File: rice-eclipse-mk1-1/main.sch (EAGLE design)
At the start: 146 parts, among them IC1 LMV321LICTRT, IC10 MCP6N11R, IC11 MCP6N11R, IC12 MCP6N11R, IC2 LMV321LICTRT, IC3 LMV321LICTRT, IC4 LMV321LICTRT, IC5 MCP6N11R, IC6 LMV321LICTRT, IC7 LMV321LICTRT, IC8 LMV321LICTRT, IC9 LMV321LICTRT, U6 1101M2S3CQE2

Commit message: Added AA filter to lowpass output.
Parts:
- added C10, C37, C40, C43, C46: 0.1UF, rcl:C-USC0805
- added C11, C36, C38, C39, C41, C42, C44, C45: 1nF, rcl:C-USC0805
- added C47, C48: ?, rcl:C-USC0805
- added IC13, IC14, IC15, IC16, IC17: LMV321LICTRT, st-microelectronics-extra:LMV321LICTRT
- added LC1, LC2, LC3, LC4, LC5, LCAA_EN, LCIN1, LCIN2, LCIN3, LCIN4, LCIN5: (no value), pinhead:PINHD-1X2
- added R11, R15, R19, R23: 24.7K, rcl:R-US_R0805
- added R12, R16, R20, R24: 164K, rcl:R-US_R0805
- added R13, R17, R21, R60: 50.6K, rcl:R-US_R0805
- added R14, R18, R22, R61: 12.6K, rcl:R-US_R0805
- added R62, R63, R64, R65: ?, rcl:R-US_R0805
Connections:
- new net +5V_LCAA: C10.1, C37.1, C40.1, C43.1, C46.1, IC13.+VS, IC14.+VS, IC15.+VS, IC16.+VS, IC17.+VS, LCAA_EN.2
- new net LC1_PREC: C31.2, IC5.OUT, LCIN1.2, RF1.1
- new net LC2_PREC: C13.2, IC10.OUT, LCIN2.2, RF2.1
- new net LC3_PREC: C33.2, IC11.OUT, LCIN3.2, RF3.1
- new net LC4_PREC: C35.2, IC12.OUT, LCIN4.2, RF4.1
- new net N$13: C11.1, R11.1, R12.2
- new net N$16: C36.1, IC13.IN+, R12.1
- new net N$17: C39.1, R15.1, R16.2
- new net N$18: C11.2, IC13.OUT, R13.1
- new net N$19: C38.1, IC14.IN+, R16.1
- new net N$20: C39.2, IC14.OUT, R17.1
- new net N$23: IC14.IN-, LC2.2, R17.2, R18.1
- new net N$24: C42.1, R19.1, R20.2
- new net N$38: C41.1, IC15.IN+, R20.1
- new net N$40: C42.2, IC15.OUT, R21.1
- new net N$44: IC15.IN-, LC3.2, R21.2, R22.1
- new net N$45: C45.1, R23.1, R24.2
- new net N$48: C44.1, IC16.IN+, R24.1
- new net N$49: C45.2, IC16.OUT, R60.1
- new net N$50: IC13.IN-, LC1.2, R13.2, R14.1
- new net N$51: IC16.IN-, LC4.2, R60.2, R61.1
- new net N$52: LCIN1.1, R11.2
- new net N$53: LCIN2.1, R15.2
- new net N$54: LCIN3.1, R19.2
- new net N$55: LCIN4.1, R23.2
- new net N$56: C48.1, R62.1, R63.2
- new net N$57: C47.1, IC17.IN+, R63.1
- new net N$58: C48.2, IC17.OUT, R64.1
- new net N$59: IC17.IN-, LC5.2, R64.2, R65.1
- new net N$60: LCIN5.1, R62.2
- net +5V: now also LCAA_EN.1
- net ADC1_A0: now also LC1.1; no longer C31.2, IC5.OUT, RF1.1
- net ADC1_A1: now also LC2.1; no longer C13.2, IC10.OUT, RF2.1
- net ADC1_A2: no longer C33.2, IC11.OUT, RF3.1
- net ADC1_A3: now also LC3.1; no longer C35.2, IC12.OUT, RF4.1
- net ADC1_A4: now also LC4.1
- net ADC1_A5: now also LC5.1
- net GND: now also C10.2, C36.2, C37.2, C38.2, C40.2, C41.2, C43.2, C44.2, C46.2, C47.2, IC13.-VS, IC14.-VS, IC15.-VS, IC16.-VS, IC17.-VS, R14.2, R18.2, R22.2, R61.2, R65.2
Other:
- note added: "2nd order Butterworth Lowpass Filter. Gain 5V/V, Cutoff 2.5KHz"
- note added: "Alternately selectable Filter stage that can be used for MK2"

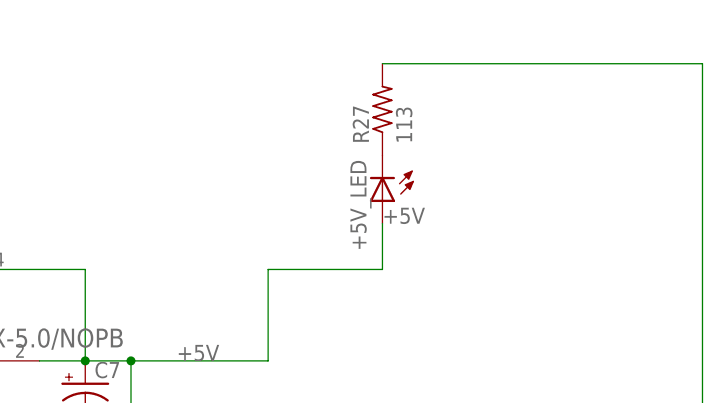
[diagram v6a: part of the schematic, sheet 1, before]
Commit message: Updated board route a bit. Rest is autorouted.
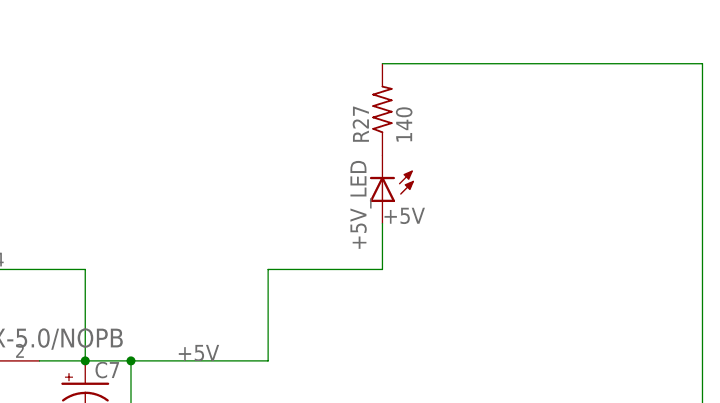
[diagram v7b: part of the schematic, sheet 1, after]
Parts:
- R27: value 113 -> 140
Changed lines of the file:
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@@
 <part name="+3.3V_LED" library="led" library_urn="urn:adsk.eagle:library:259" deviceset="LED" device="5MM" package3d_urn="urn:adsk.eagle:package:15799/1"/>
 <part name="R26" library="resistor" library_urn="urn:adsk.eagle:library:348" deviceset="R-US_" device="R0805" package3d_urn="urn:adsk.eagle:package:26059/1" value="530"/>
-<part name="R27" library="resistor" library_urn="urn:adsk.eagle:library:348" deviceset="R-US_" device="R0805" value="113"/>
+<part name="R27" library="resistor" library_urn="urn:adsk.eagle:library:348" deviceset="R-US_" device="R0805" value="140"/>
 <part name="R28" library="resistor" library_urn="urn:adsk.eagle:library:348" deviceset="R-US_" device="R0805" value="39"/>
 <part name="X4" library="con-phoenix-254" library_urn="urn:adsk.eagle:library:172" deviceset="MPT8" device="" package3d_urn="urn:adsk.eagle:package:9329/1"/>

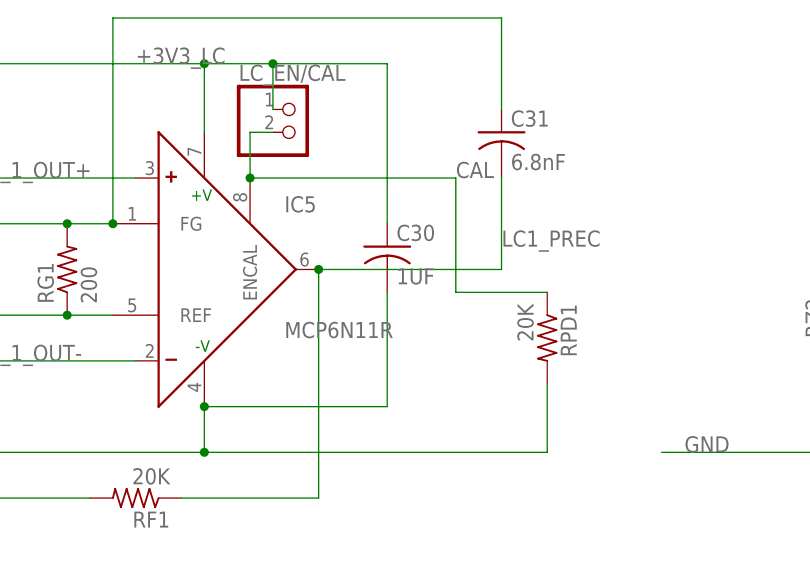
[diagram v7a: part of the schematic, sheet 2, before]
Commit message: Added final routing for version 1.1.
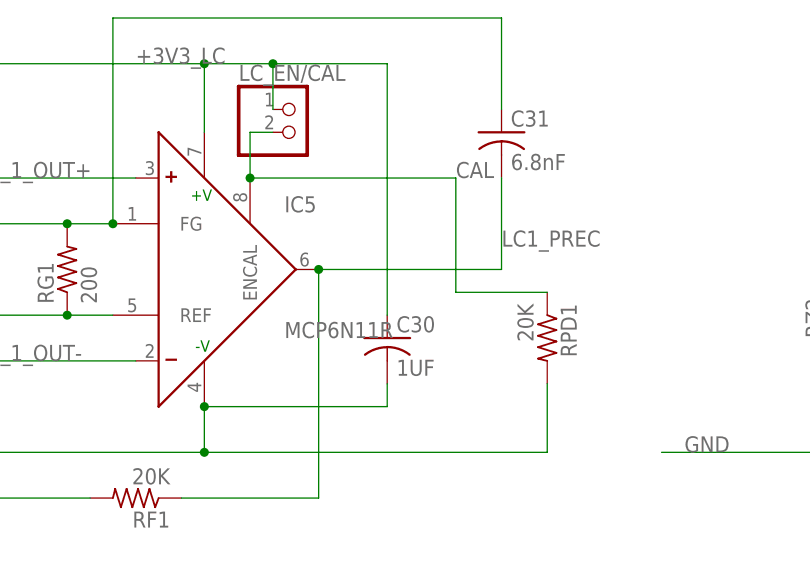
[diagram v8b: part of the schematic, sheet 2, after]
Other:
- moved on the sheet: C30
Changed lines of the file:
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@@
 <instance part="RG1" gate="G$1" x="60.96" y="137.16" rot="R90"/>
 <instance part="RF1" gate="G$1" x="68.58" y="111.76" rot="R180"/>
-<instance part="C30" gate="G$1" x="96.52" y="139.7"/>
+<instance part="C30" gate="G$1" x="96.52" y="129.54"/>
 <instance part="RZ1" gate="G$1" x="40.64" y="132.08"/>
 <instance part="C31" gate="G$1" x="109.22" y="152.4"/>
@@
 <wire x1="40.64" y1="124.46" x2="40.64" y2="116.84" width="0.1524" layer="91"/>
 <pinref part="C30" gate="G$1" pin="2"/>
-<wire x1="96.52" y1="134.62" x2="96.52" y2="121.92" width="0.1524" layer="91"/>
+<wire x1="96.52" y1="124.46" x2="96.52" y2="121.92" width="0.1524" layer="91"/>
 <wire x1="96.52" y1="121.92" x2="76.2" y2="121.92" width="0.1524" layer="91"/>
 <junction x="76.2" y="121.92"/>
@@
 <wire x1="40.64" y1="160.02" x2="76.2" y2="160.02" width="0.1524" layer="91"/>
 <pinref part="C30" gate="G$1" pin="1"/>
-<wire x1="96.52" y1="142.24" x2="96.52" y2="160.02" width="0.1524" layer="91"/>
+<wire x1="96.52" y1="132.08" x2="96.52" y2="160.02" width="0.1524" layer="91"/>
 <wire x1="96.52" y1="160.02" x2="83.82" y2="160.02" width="0.1524" layer="91"/>
 <junction x="83.82" y="160.02"/>
